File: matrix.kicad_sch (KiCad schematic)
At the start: 285 parts, among them SW2 SW_SPDT, SW3 SW_SPDT

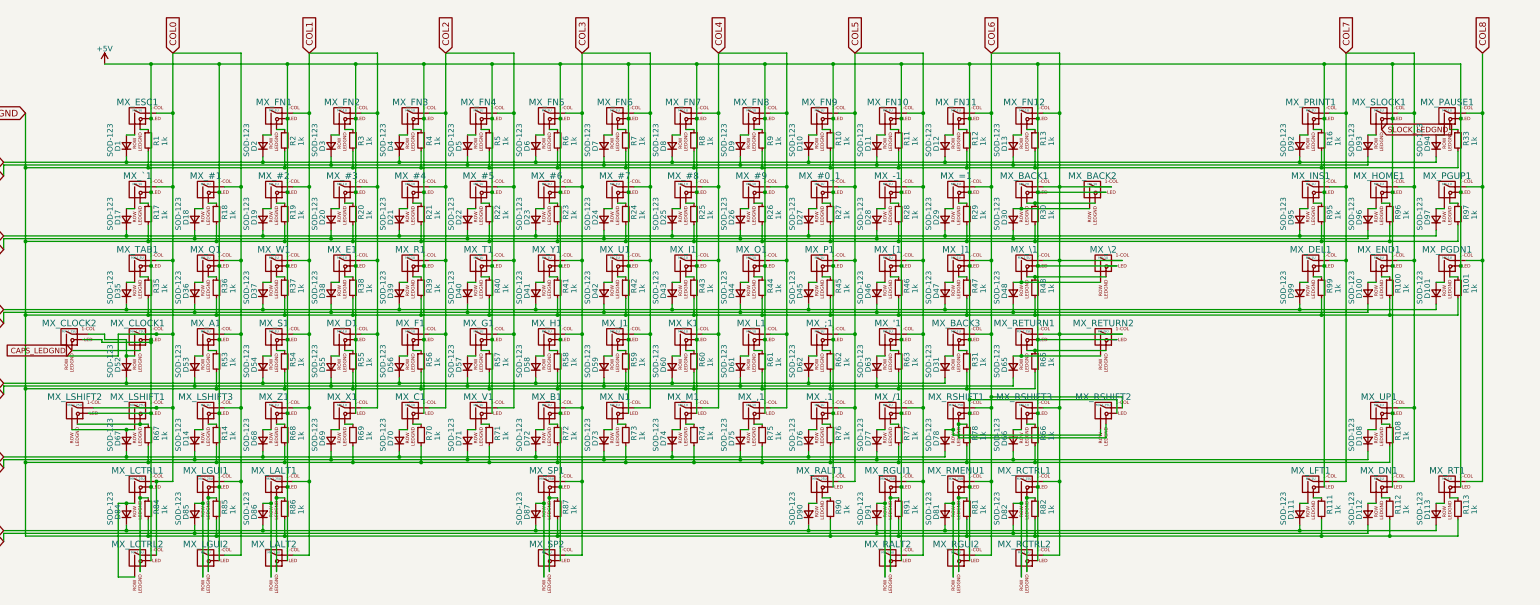
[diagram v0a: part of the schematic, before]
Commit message: Made the project portable
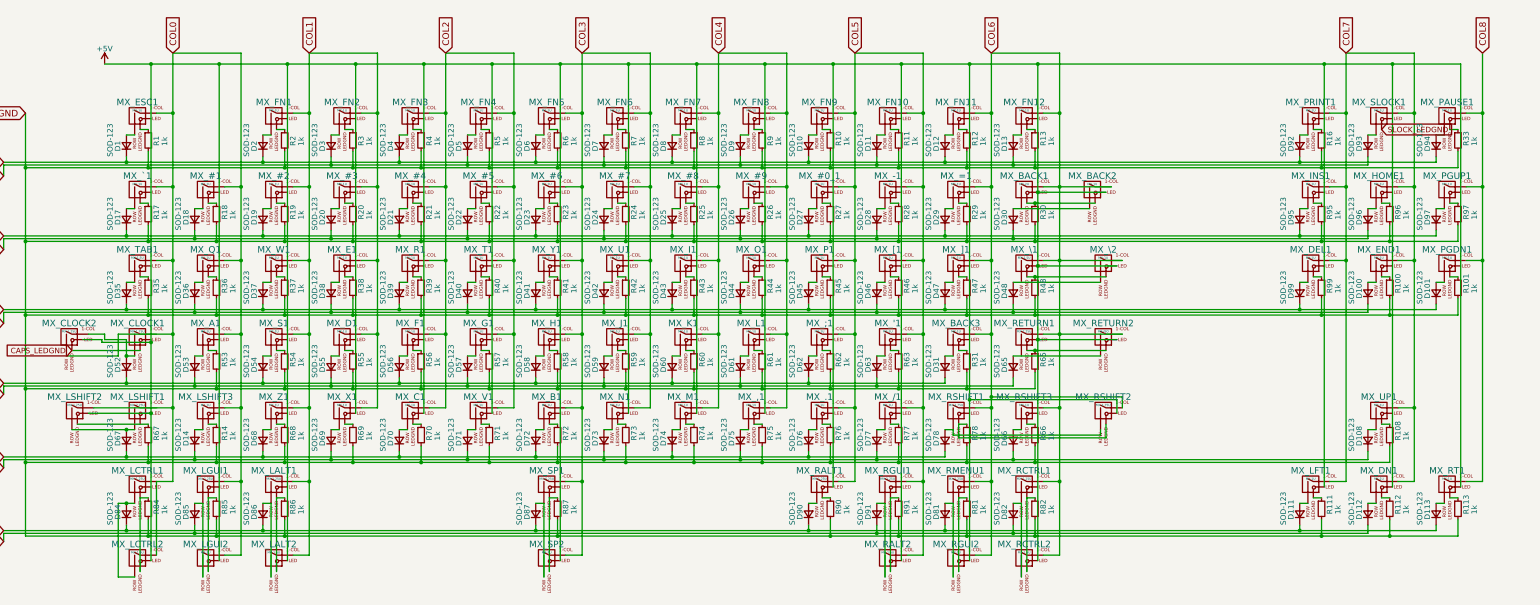
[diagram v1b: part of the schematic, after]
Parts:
- D1, D10, D100, D101, D108, D11, D111, D112, D113, D12, D13, D14, D17, D18, D19, D2, D20, D21, D22, D23, D24, D25, D26, D27, D28, D29, D3, D30, D31, D35, D36, D37, D38, D39, D4, D40, D41, D42, D43, D44, D45, D46, D47, D48, D5, D52, D53, D54, D55, D56, D57, D58, D59, D6, D60, D61, D62, D63, D65, D66, D67, D68, D69, D7, D70, D71, D72, D73, D74, D75, D76, D77, D78, D8, D81, D82, D84, D85, D86, D87, D9, D90, D91, D92, D93, D94, D95, D96, D97, D99: footprint locallib:D_SOD-123 -> KBD8X_MK2_Components:D_SOD-123; symbol Device:D_Small -> KBD8X_MK2_Components:D_Small
- MX_#0_1, MX_#1, MX_#2, MX_#3, MX_#4, MX_#5, MX_#6, MX_#7, MX_#8, MX_#9, MX_'1, MX_,1, MX_-1, MX_.1, MX_/1, MX_;1, MX_=1, MX_A1, MX_B1, MX_BACK2, MX_BACK3, MX_C1, MX_D1, MX_DEL1, MX_DN1, MX_E1, MX_END1, MX_ESC1, MX_F1, MX_FN1, MX_FN10, MX_FN11, MX_FN12, MX_FN2, MX_FN3, MX_FN4, MX_FN5, MX_FN6, MX_FN7, MX_FN8, MX_FN9, MX_G1, MX_H1, MX_HOME1, MX_I1, MX_INS1, MX_J1, MX_K1, MX_L1, MX_LFT1, MX_LSHIFT3, MX_M1, MX_N1, MX_O1, MX_P1, MX_PAUSE1, MX_PGDN1, MX_PGUP1, MX_PRINT1, MX_Q1, MX_R1, MX_RSHIFT3, MX_RT1, MX_S1, MX_SLOCK1, MX_T1, MX_U1, MX_UP1, MX_V1, MX_W1, MX_X1, MX_Y1, MX_Z1, MX_[1, MX_\2, MX_]1, MX_`1: footprint MX_Alps_Hybrid:MXOnly-1U -> KBD8X_MK2_Switches:MXOnly-1U; symbol MX_Alps_Hybrids:MX-1U -> KBD8X_MK2_Switches:MX-1U
- MX_BACK1: footprint MX_Alps_Hybrid:MXOnly-2U -> KBD8X_MK2_Switches:MXOnly-2U; symbol MX_Alps_Hybrids:MX-2U -> KBD8X_MK2_Switches:MX-2U
- MX_CLOCK1: footprint MX_Alps_Hybrid:MXOnly-1.75U -> KBD8X_MK2_Switches:MXOnly-1.75U; symbol MX_Alps_Hybrids:MX-1.75U -> KBD8X_MK2_Switches:MX-1.75U
- MX_CLOCK2, MX_RGUI1: footprint MX_Alps_Hybrid:MXOnly-1.25U-FLIPPED -> KBD8X_MK2_Switches:MXOnly-1.25U-FLIPPED; symbol MX_Alps_Hybrids:MX-1.25U -> KBD8X_MK2_Switches:MX-1.25U
- MX_LALT1, MX_LGUI1, MX_RALT1: footprint MX_Alps_Hybrid:MXOnly-1.25U -> KBD8X_MK2_Switches:MXOnly-1.25U; symbol MX_Alps_Hybrids:MX-1.25U -> KBD8X_MK2_Switches:MX-1.25U
- MX_LALT2, MX_LCTRL2: footprint MX_Alps_Hybrid:MXOnly-1.5U-FLIPPED -> KBD8X_MK2_Switches:MXOnly-1.5U-FLIPPED; symbol MX_Alps_Hybrids:MX-1.5U -> KBD8X_MK2_Switches:MX-1.5U
- MX_LCTRL1: footprint MX_Alps_Hybrid:MXOnly-1.25U -> KBD8X_MK2_Switches:MXOnly-1.25U; symbol MX_Alps_Hybrids:MX-1U -> KBD8X_MK2_Switches:MX-1U
- MX_LGUI2: footprint MX_Alps_Hybrid:MXOnly-1U-FLIPPED -> KBD8X_MK2_Switches:MXOnly-1U-FLIPPED; symbol MX_Alps_Hybrids:MX-1.5U -> KBD8X_MK2_Switches:MX-1.5U
- MX_LSHIFT1, MX_RETURN1: footprint MX_Alps_Hybrid:MXOnly-2.25U -> KBD8X_MK2_Switches:MXOnly-2.25U; symbol MX_Alps_Hybrids:MX-2.25U -> KBD8X_MK2_Switches:MX-2.25U
- MX_LSHIFT2: footprint MX_Alps_Hybrid:MXOnly-1.25U -> KBD8X_MK2_Switches:MXOnly-1.25U; symbol MX_Alps_Hybrids:MX-2.25U -> KBD8X_MK2_Switches:MX-2.25U
- MX_RALT2, MX_RCTRL2, MX_TAB1, MX_\1: footprint MX_Alps_Hybrid:MXOnly-1.5U -> KBD8X_MK2_Switches:MXOnly-1.5U; symbol MX_Alps_Hybrids:MX-1.5U -> KBD8X_MK2_Switches:MX-1.5U
- MX_RCTRL1, MX_RMENU1: footprint MX_Alps_Hybrid:MXOnly-1.25U-FLIPPED -> KBD8X_MK2_Switches:MXOnly-1.25U-FLIPPED; symbol MX_Alps_Hybrids:MX-1U -> KBD8X_MK2_Switches:MX-1U
- MX_RETURN2: footprint MX_Alps_Hybrid:MXOnly-ISO-ROTATED-ReversedStabilizers -> KBD8X_MK2_Switches:MXOnly-ISO-ROTATED-ReversedStabilizers; symbol MX_Alps_Hybrids:MX-2.25U -> KBD8X_MK2_Switches:MX-2.25U
- MX_RGUI2: footprint MX_Alps_Hybrid:MXOnly-1U -> KBD8X_MK2_Switches:MXOnly-1U; symbol MX_Alps_Hybrids:MX-1.5U -> KBD8X_MK2_Switches:MX-1.5U
- MX_RSHIFT1: footprint MX_Alps_Hybrid:MXOnly-2.75U -> KBD8X_MK2_Switches:MXOnly-2.75U; symbol MX_Alps_Hybrids:MX-1U -> KBD8X_MK2_Switches:MX-1U
- MX_RSHIFT2: footprint MX_Alps_Hybrid:MXOnly-1.75U -> KBD8X_MK2_Switches:MXOnly-1.75U; symbol MX_Alps_Hybrids:MX-1U -> KBD8X_MK2_Switches:MX-1U
- MX_SP1: footprint MX_Alps_Hybrid:MXOnly-6.25U-ReversedStabilizers -> KBD8X_MK2_Switches:MXOnly-6.25U-ReversedStabilizers; symbol MX_Alps_Hybrids:MX-6.25U -> KBD8X_MK2_Switches:MX-6.25U
- MX_SP2: footprint MX_Alps_Hybrid:MXOnly-7U-ReversedStabilizers -> KBD8X_MK2_Switches:MXOnly-7U-ReversedStabilizers; symbol MX_Alps_Hybrids:MX-7U -> KBD8X_MK2_Switches:MX-7U
- R1, R10, R100, R101, R108, R11, R111, R112, R113, R12, R13, R14, R16, R17, R18, R19, R2, R20, R21, R22, R23, R24, R25, R26, R27, R28, R29, R3, R30, R31, R32, R33, R35, R36, R37, R38, R39, R4, R40, R41, R42, R43, R44, R45, R46, R47, R48, R5, R52, R53, R54, R55, R56, R57, R58, R59, R6, R60, R61, R62, R63, R65, R66, R67, R68, R69, R7, R70, R71, R72, R73, R74, R75, R76, R77, R78, R8, R81, R82, R84, R85, R86, R87, R9, R90, R91, R95, R96, R97, R99: footprint locallib:R_0603 -> KBD8X_MK2_Components:R_0603; symbol Device:R_Small -> KBD8X_MK2_Components:R_Small
- SW2, SW3: footprint Buttons_Switches_SMD:SW_SPDT_PCM12 -> KBD8X_MK2_Components:SW_SPDT_PCM12; symbol Switch:SW_SPDT -> KBD8X_MK2_Components:SW_SPDT
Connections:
- net +5V: no longer MX_#0_1.3 (LED), MX_#1.3 (LED), MX_#2.3 (LED), MX_#3.3 (LED), MX_#4.3 (LED), MX_#5.3 (LED), MX_#6.3 (LED), MX_#7.3 (LED), MX_#8.3 (LED), MX_#9.3 (LED), MX_'1.3 (LED), MX_-1.3 (LED), MX_.1.3 (LED), MX_/1.3 (LED), MX_;1.3 (LED), MX_=1.3 (LED), MX_A1.3 (LED), MX_B1.3 (LED), MX_BACK3.3 (LED), MX_CLOCK1.3 (LED), MX_D1.3 (LED), MX_DEL1.3 (LED), MX_E1.3 (LED), MX_END1.3 (LED), MX_ESC1.3 (LED), MX_F1.3 (LED), MX_FN1.3 (LED), MX_FN10.3 (LED), MX_FN11.3 (LED), MX_FN12.3 (LED), MX_FN2.3 (LED), MX_FN3.3 (LED), MX_FN4.3 (LED), MX_FN5.3 (LED), MX_FN6.3 (LED), MX_FN7.3 (LED), MX_FN8.3 (LED), MX_FN9.3 (LED), MX_G1.3 (LED), MX_H1.3 (LED), MX_HOME1.3 (LED), MX_I1.3 (LED), MX_INS1.3 (LED), MX_J1.3 (LED), MX_K1.3 (LED), MX_L1.3 (LED), MX_LALT1.3 (LED), MX_LCTRL1.3 (LED), MX_LGUI1.3 (LED), MX_LSHIFT3.3 (LED), MX_O1.3 (LED), MX_P1.3 (LED), MX_PAUSE1.3 (LED), MX_PGDN1.3 (LED), MX_PGUP1.3 (LED), MX_PRINT1.3 (LED), MX_Q1.3 (LED), MX_R1.3 (LED), MX_RCTRL1.3 (LED), MX_RGUI1.3 (LED), MX_RMENU1.3 (LED), MX_RSHIFT1.3 (LED), MX_RSHIFT3.3 (LED), MX_S1.3 (LED), MX_SLOCK1.3 (LED), MX_SP1.3 (LED), MX_T1.3 (LED), MX_TAB1.3 (LED), MX_U1.3 (LED), MX_UP1.3 (LED), MX_W1.3 (LED), MX_Y1.3 (LED), MX_Z1.3 (LED), MX_[1.3 (LED), MX_]1.3 (LED), MX_`1.3 (LED)
- net COL0: no longer MX_CLOCK1.1 (COL), MX_LSHIFT1.1 (COL)
- net at D30.2 (A), MX_BACK2.2 (ROW): no longer MX_BACK1.2 (ROW)
- net at D48.2 (A), MX_\2.2 (ROW): no longer MX_\1.2 (ROW)
- net at MX_LSHIFT2.4 (LEDGND), R67.1: no longer MX_LSHIFT1.4 (LEDGND)
- net at D65.2 (A), MX_RETURN2.2 (ROW): no longer MX_RETURN1.2 (ROW)

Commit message: Rearrenged schematics items
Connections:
- net +5V: now also MX_#0_1.3 (LED), MX_#1.3 (LED), MX_#2.3 (LED), MX_#3.3 (LED), MX_#4.3 (LED), MX_#5.3 (LED), MX_#6.3 (LED), MX_#7.3 (LED), MX_#8.3 (LED), MX_#9.3 (LED), MX_'1.3 (LED), MX_-1.3 (LED), MX_.1.3 (LED), MX_/1.3 (LED), MX_;1.3 (LED), MX_=1.3 (LED), MX_A1.3 (LED), MX_B1.3 (LED), MX_BACK3.3 (LED), MX_CLOCK1.3 (LED), MX_D1.3 (LED), MX_DEL1.3 (LED), MX_E1.3 (LED), MX_END1.3 (LED), MX_ESC1.3 (LED), MX_F1.3 (LED), MX_FN1.3 (LED), MX_FN10.3 (LED), MX_FN11.3 (LED), MX_FN12.3 (LED), MX_FN2.3 (LED), MX_FN3.3 (LED), MX_FN4.3 (LED), MX_FN5.3 (LED), MX_FN6.3 (LED), MX_FN7.3 (LED), MX_FN8.3 (LED), MX_FN9.3 (LED), MX_G1.3 (LED), MX_H1.3 (LED), MX_HOME1.3 (LED), MX_I1.3 (LED), MX_INS1.3 (LED), MX_J1.3 (LED), MX_K1.3 (LED), MX_L1.3 (LED), MX_LALT1.3 (LED), MX_LCTRL1.3 (LED), MX_LGUI1.3 (LED), MX_LSHIFT3.3 (LED), MX_O1.3 (LED), MX_P1.3 (LED), MX_PAUSE1.3 (LED), MX_PGDN1.3 (LED), MX_PGUP1.3 (LED), MX_PRINT1.3 (LED), MX_Q1.3 (LED), MX_R1.3 (LED), MX_RCTRL1.3 (LED), MX_RGUI1.3 (LED), MX_RMENU1.3 (LED), MX_RSHIFT1.3 (LED), MX_RSHIFT3.3 (LED), MX_S1.3 (LED), MX_SLOCK1.3 (LED), MX_SP1.3 (LED), MX_T1.3 (LED), MX_TAB1.3 (LED), MX_U1.3 (LED), MX_UP1.3 (LED), MX_W1.3 (LED), MX_Y1.3 (LED), MX_Z1.3 (LED), MX_[1.3 (LED), MX_]1.3 (LED), MX_`1.3 (LED)
- net COL0: now also MX_CLOCK1.1 (COL), MX_LSHIFT1.1 (COL)
- net at MX_BACK1.2 (ROW): now also D30.2 (A), MX_BACK2.2 (ROW)
- net at MX_\1.2 (ROW): now also D48.2 (A), MX_\2.2 (ROW)
- net at MX_LSHIFT1.4 (LEDGND): now also MX_LSHIFT2.4 (LEDGND), R67.1
- net at MX_RETURN1.2 (ROW): now also D65.2 (A), MX_RETURN2.2 (ROW)
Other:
- moved on the sheet: D1, D10, D100, D101, D108, D11, D111, D112, D113, D12, D13, D14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

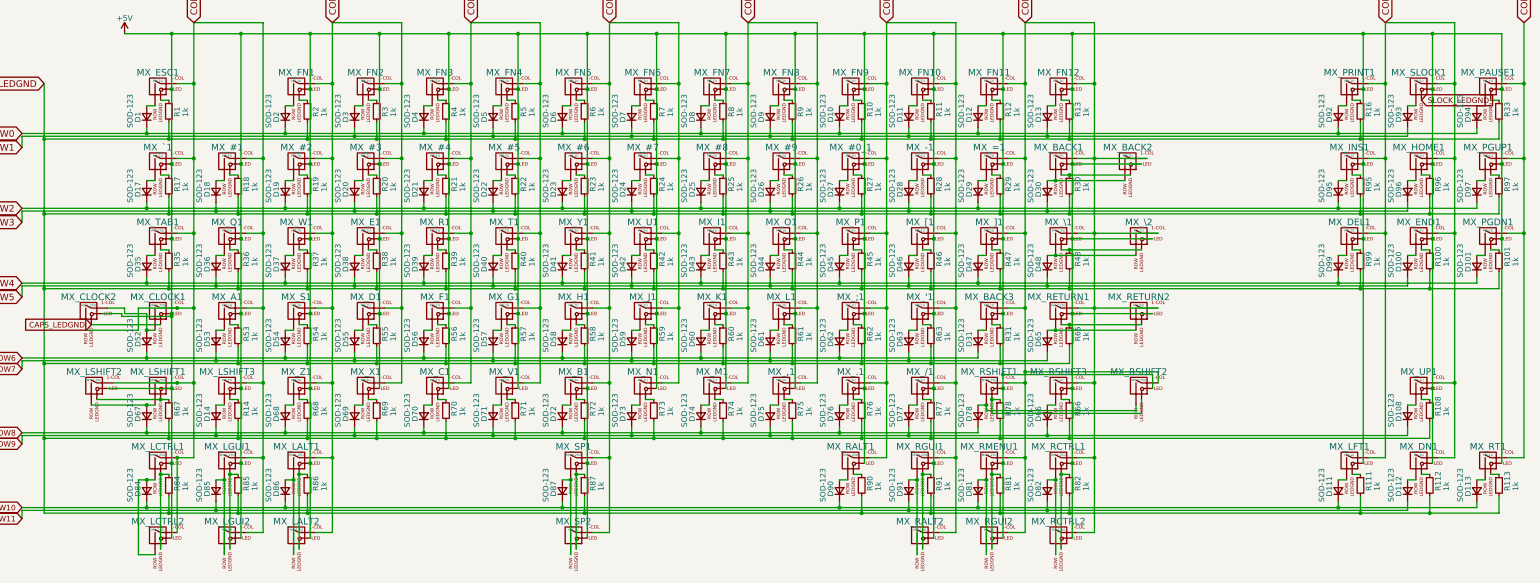
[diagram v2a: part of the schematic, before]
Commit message: Updated symbols used in the schematics
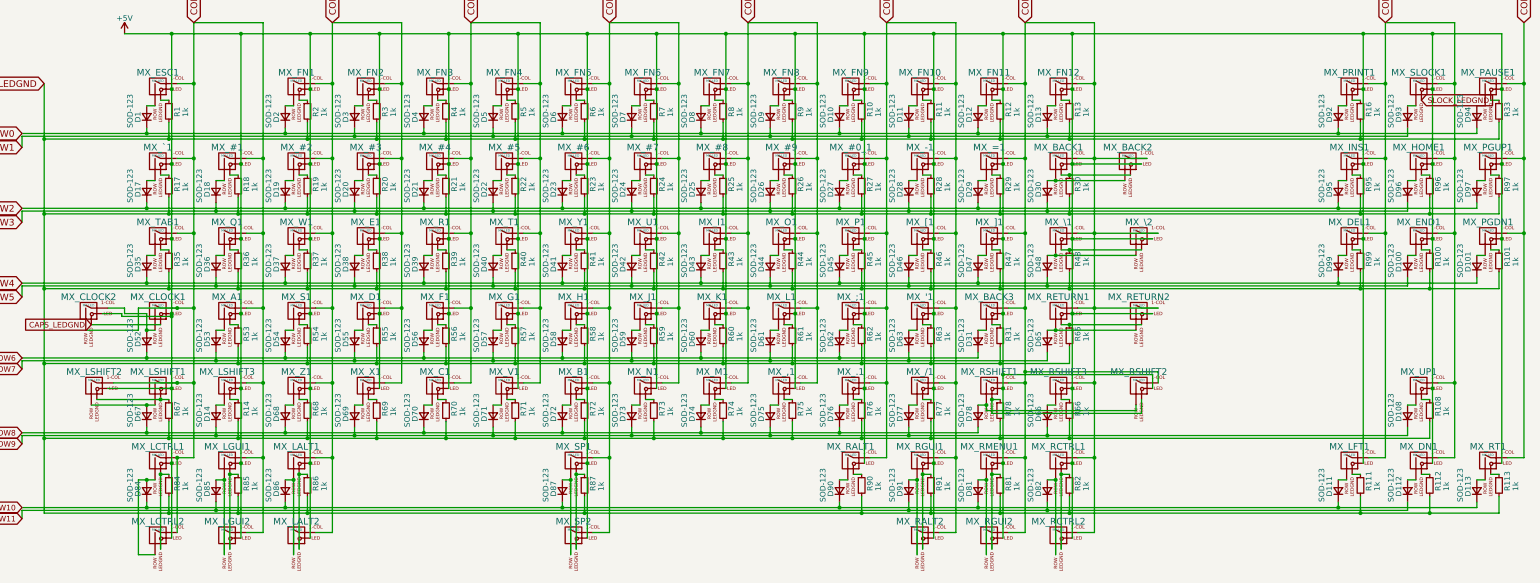
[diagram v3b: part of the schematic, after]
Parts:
- MX_#0_1, MX_#1, MX_#2, MX_#3, MX_#4, MX_#5, MX_#6, MX_#7, MX_#8, MX_#9, MX_'1, MX_,1, MX_-1, MX_.1, MX_/1, MX_;1, MX_=1, MX_A1, MX_B1, MX_BACK2, MX_BACK3, MX_C1, MX_D1, MX_DEL1, MX_DN1, MX_E1, MX_END1, MX_ESC1, MX_F1, MX_FN1, MX_FN10, MX_FN11, MX_FN12, MX_FN2, MX_FN3, MX_FN4, MX_FN5, MX_FN6, MX_FN7, MX_FN8, MX_FN9, MX_G1, MX_H1, MX_HOME1, MX_I1, MX_INS1, MX_J1, MX_K1, MX_L1, MX_LFT1, MX_LSHIFT3, MX_M1, MX_N1, MX_O1, MX_P1, MX_PAUSE1, MX_PGDN1, MX_PGUP1, MX_PRINT1, MX_Q1, MX_R1, MX_RSHIFT3, MX_RT1, MX_S1, MX_SLOCK1, MX_T1, MX_U1, MX_UP1, MX_V1, MX_W1, MX_X1, MX_Y1, MX_Z1, MX_[1, MX_\2, MX_]1, MX_`1: value MX-1U -> MX-LED; symbol KBD8X_MK2_Switches:MX-1U -> KBD8X_MK2_Switches:MX-LED
- MX_BACK1: value MX-2U -> MX-LED; symbol KBD8X_MK2_Switches:MX-2U -> KBD8X_MK2_Switches:MX-LED
- MX_CLOCK1: value MX-1.75U -> MX-LED; symbol KBD8X_MK2_Switches:MX-1.75U -> KBD8X_MK2_Switches:MX-LED
- MX_CLOCK2, MX_LALT1, MX_LGUI1, MX_RALT1, MX_RGUI1: value MX-1.25U -> MX-LED; symbol KBD8X_MK2_Switches:MX-1.25U -> KBD8X_MK2_Switches:MX-LED
- MX_LALT2, MX_LCTRL2, MX_RALT2, MX_RCTRL2, MX_TAB1, MX_\1: value MX-1.5U -> MX-LED; symbol KBD8X_MK2_Switches:MX-1.5U -> KBD8X_MK2_Switches:MX-LED
- MX_LCTRL1, MX_RCTRL1, MX_RMENU1: value MX-1.25U -> MX-LED; symbol KBD8X_MK2_Switches:MX-1U -> KBD8X_MK2_Switches:MX-LED
- MX_LGUI2, MX_RGUI2: value MX-1U -> MX-LED; symbol KBD8X_MK2_Switches:MX-1.5U -> KBD8X_MK2_Switches:MX-LED
- MX_LSHIFT1, MX_RETURN1: value MX-2.25U -> MX-LED; symbol KBD8X_MK2_Switches:MX-2.25U -> KBD8X_MK2_Switches:MX-LED
- MX_LSHIFT2: value MX-1.25U -> MX-LED; symbol KBD8X_MK2_Switches:MX-2.25U -> KBD8X_MK2_Switches:MX-LED
- MX_RETURN2: value MX-ISO -> MX-LED; symbol KBD8X_MK2_Switches:MX-2.25U -> KBD8X_MK2_Switches:MX-LED
- MX_RSHIFT1: value MX-2.75U -> MX-LED; symbol KBD8X_MK2_Switches:MX-1U -> KBD8X_MK2_Switches:MX-LED
- MX_RSHIFT2: value MX-1.75U -> MX-LED; symbol KBD8X_MK2_Switches:MX-1U -> KBD8X_MK2_Switches:MX-LED
- MX_SP1: value MX-6.25U -> MX-LED; symbol KBD8X_MK2_Switches:MX-6.25U -> KBD8X_MK2_Switches:MX-LED
- MX_SP2: value MX-7U -> MX-LED; symbol KBD8X_MK2_Switches:MX-7U -> KBD8X_MK2_Switches:MX-LED

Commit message: Removed leds and unnecessary resistors
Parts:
- removed R1, R10, R100, R101, R108, R11, R111, R112, R113, R12, R13, R14, R16, R17, R18, R19, R2, R20, R21, R22, R23, R24, R25, R26, R27, R28, R29, R3, R30, R31, R33, R35, R36, R37, R38, R39, R4, R40, R41, R42, R43, R44, R45, R46, R47, R48, R5, R53, R54, R55, R56, R57, R58, R59, R6, R60, R61, R62, R63, R65, R66, R67, R68, R69, R7, R70, R71, R72, R73, R74, R75, R76, R77, R78, R8, R81, R82, R84, R85, R86, R87, R9, R90, R91, R95, R96, R97, R99: 1k, KBD8X_MK2_Components:R_0603, symbol KBD8X_MK2_Components:R_Small
- removed SW2, SW3: SW_SPDT, KBD8X_MK2_Components:SW_SPDT_PCM12, symbol KBD8X_MK2_Components:SW_SPDT
- MX_#0_1, MX_#1, MX_#2, MX_#3, MX_#4, MX_#5, MX_#6, MX_#7, MX_#8, MX_#9, MX_'1, MX_,1, MX_-1, MX_.1, MX_/1, MX_;1, MX_=1, MX_A1, MX_B1, MX_BACK2, MX_BACK3, MX_C1, MX_D1, MX_DEL1, MX_DN1, MX_E1, MX_END1, MX_ESC1, MX_F1, MX_FN1, MX_FN10, MX_FN11, MX_FN12, MX_FN2, MX_FN3, MX_FN4, MX_FN5, MX_FN6, MX_FN7, MX_FN8, MX_FN9, MX_G1, MX_H1, MX_HOME1, MX_I1, MX_INS1, MX_J1, MX_K1, MX_L1, MX_LFT1, MX_LSHIFT3, MX_M1, MX_N1, MX_O1, MX_P1, MX_PAUSE1, MX_PGDN1, MX_PGUP1, MX_PRINT1, MX_Q1, MX_R1, MX_RGUI2, MX_RSHIFT3, MX_RT1, MX_S1, MX_T1, MX_U1, MX_UP1, MX_V1, MX_W1, MX_X1, MX_Y1, MX_Z1, MX_[1, MX_\2, MX_]1, MX_`1: value MX-LED -> MX-NoLED; footprint KBD8X_MK2_Switches:MXOnly-1U -> KBD8X_MK2_Switches:MXOnly-1U-NoLED; symbol KBD8X_MK2_Switches:MX-LED -> KBD8X_MK2_Switches:MX-NoLED
- MX_BACK1: value MX-LED -> MX-NoLED; footprint KBD8X_MK2_Switches:MXOnly-2U -> KBD8X_MK2_Switches:MXOnly-2U-NoLED; symbol KBD8X_MK2_Switches:MX-LED -> KBD8X_MK2_Switches:MX-NoLED
- MX_LALT1, MX_LCTRL1, MX_LGUI1, MX_LSHIFT2, MX_RALT1: value MX-LED -> MX-NoLED; footprint KBD8X_MK2_Switches:MXOnly-1.25U -> KBD8X_MK2_Switches:MXOnly-1.25U-NoLED; symbol KBD8X_MK2_Switches:MX-LED -> KBD8X_MK2_Switches:MX-NoLED
- MX_LALT2, MX_LCTRL2: value MX-LED -> MX-NoLED; footprint KBD8X_MK2_Switches:MXOnly-1.5U-FLIPPED -> KBD8X_MK2_Switches:MXOnly-1.5U-NoLED; symbol KBD8X_MK2_Switches:MX-LED -> KBD8X_MK2_Switches:MX-NoLED
- MX_LGUI2: value MX-LED -> MX-NoLED; footprint KBD8X_MK2_Switches:MXOnly-1U-FLIPPED -> KBD8X_MK2_Switches:MXOnly-1U-NoLED; symbol KBD8X_MK2_Switches:MX-LED -> KBD8X_MK2_Switches:MX-NoLED
- MX_LSHIFT1, MX_RETURN1: value MX-LED -> MX-NoLED; footprint KBD8X_MK2_Switches:MXOnly-2.25U -> KBD8X_MK2_Switches:MXOnly-2.25U-NoLED; symbol KBD8X_MK2_Switches:MX-LED -> KBD8X_MK2_Switches:MX-NoLED
- MX_RALT2, MX_RCTRL2, MX_TAB1, MX_\1: value MX-LED -> MX-NoLED; footprint KBD8X_MK2_Switches:MXOnly-1.5U -> KBD8X_MK2_Switches:MXOnly-1.5U-NoLED; symbol KBD8X_MK2_Switches:MX-LED -> KBD8X_MK2_Switches:MX-NoLED
- MX_RCTRL1, MX_RGUI1, MX_RMENU1: value MX-LED -> MX-NoLED; footprint KBD8X_MK2_Switches:MXOnly-1.25U-FLIPPED -> KBD8X_MK2_Switches:MXOnly-1.25U-NoLED; symbol KBD8X_MK2_Switches:MX-LED -> KBD8X_MK2_Switches:MX-NoLED
- MX_RETURN2: value MX-LED -> MX-NoLED; footprint KBD8X_MK2_Switches:MXOnly-ISO-ROTATED-ReversedStabilizers -> KBD8X_MK2_Switches:MXOnly-ISO-ROTATED-ReversedStabilizers-NoLED; symbol KBD8X_MK2_Switches:MX-LED -> KBD8X_MK2_Switches:MX-NoLED
- MX_RSHIFT1: value MX-LED -> MX-NoLED; footprint KBD8X_MK2_Switches:MXOnly-2.75U -> KBD8X_MK2_Switches:MXOnly-2.75U-NoLED; symbol KBD8X_MK2_Switches:MX-LED -> KBD8X_MK2_Switches:MX-NoLED
- MX_RSHIFT2: value MX-LED -> MX-NoLED; footprint KBD8X_MK2_Switches:MXOnly-1.75U -> KBD8X_MK2_Switches:MXOnly-1.75U-NoLED; symbol KBD8X_MK2_Switches:MX-LED -> KBD8X_MK2_Switches:MX-NoLED
- MX_SP1: value MX-LED -> MX-NoLED; footprint KBD8X_MK2_Switches:MXOnly-6.25U-ReversedStabilizers -> KBD8X_MK2_Switches:MXOnly-6.25U-ReversedStabilizers-NoLED; symbol KBD8X_MK2_Switches:MX-LED -> KBD8X_MK2_Switches:MX-NoLED
- MX_SP2: value MX-LED -> MX-NoLED; footprint KBD8X_MK2_Switches:MXOnly-7U-ReversedStabilizers -> KBD8X_MK2_Switches:MXOnly-7U-ReversedStabilizers-NoLED; symbol KBD8X_MK2_Switches:MX-LED -> KBD8X_MK2_Switches:MX-NoLED
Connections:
- net +5V: no longer MX_#0_1.3 (LED), MX_#1.3 (LED), MX_#2.3 (LED), MX_#3.3 (LED), MX_#4.3 (LED), MX_#5.3 (LED), MX_#6.3 (LED), MX_#7.3 (LED), MX_#8.3 (LED), MX_#9.3 (LED), MX_'1.3 (LED), MX_,1.3 (LED), MX_-1.3 (LED), MX_.1.3 (LED), MX_/1.3 (LED), MX_;1.3 (LED), MX_=1.3 (LED), MX_A1.3 (LED), MX_B1.3 (LED), MX_BACK1.3 (LED), MX_BACK2.3 (LED), MX_BACK3.3 (LED), MX_C1.3 (LED), MX_D1.3 (LED), MX_DEL1.3 (LED), MX_DN1.3 (LED), MX_E1.3 (LED), MX_END1.3 (LED), MX_ESC1.3 (LED), MX_F1.3 (LED), MX_FN1.3 (LED), MX_FN10.3 (LED), MX_FN11.3 (LED), MX_FN12.3 (LED), MX_FN2.3 (LED), MX_FN3.3 (LED), MX_FN4.3 (LED), MX_FN5.3 (LED), MX_FN6.3 (LED), MX_FN7.3 (LED), MX_FN8.3 (LED), MX_FN9.3 (LED), MX_G1.3 (LED), MX_H1.3 (LED), MX_HOME1.3 (LED), MX_I1.3 (LED), MX_INS1.3 (LED), MX_J1.3 (LED), MX_K1.3 (LED), MX_L1.3 (LED), MX_LALT1.3 (LED), MX_LALT2.3 (LED), MX_LCTRL1.3 (LED), MX_LCTRL2.3 (LED), MX_LFT1.3 (LED), MX_LGUI1.3 (LED), MX_LGUI2.3 (LED), MX_LSHIFT1.3 (LED), MX_LSHIFT2.3 (LED), MX_LSHIFT3.3 (LED), MX_M1.3 (LED), MX_N1.3 (LED), MX_O1.3 (LED), MX_P1.3 (LED), MX_PAUSE1.3 (LED), MX_PGDN1.3 (LED), MX_PGUP1.3 (LED), MX_PRINT1.3 (LED), MX_Q1.3 (LED), MX_R1.3 (LED), MX_RALT1.3 (LED), MX_RALT2.3 (LED), MX_RCTRL1.3 (LED), MX_RCTRL2.3 (LED), MX_RETURN1.3 (LED), MX_RETURN2.3 (LED), MX_RGUI1.3 (LED), MX_RGUI2.3 (LED), MX_RMENU1.3 (LED), MX_RSHIFT1.3 (LED), MX_RSHIFT2.3 (LED), MX_RSHIFT3.3 (LED), MX_RT1.3 (LED), MX_S1.3 (LED), MX_SP1.3 (LED), MX_SP2.3 (LED), MX_T1.3 (LED), MX_TAB1.3 (LED), MX_U1.3 (LED), MX_UP1.3 (LED), MX_V1.3 (LED), MX_W1.3 (LED), MX_X1.3 (LED), MX_Y1.3 (LED), MX_Z1.3 (LED), MX_[1.3 (LED), MX_\1.3 (LED), MX_\2.3 (LED), MX_]1.3 (LED), MX_`1.3 (LED)
- net CAPS_IND: now also R52.2
- net SLOCK_IND: now also R32.1
- net CAPS_LEDGND: no longer names the net of MX_CLOCK1.4 (LEDGND), MX_CLOCK2.4 (LEDGND), R52.1
- net SLOCK_LEDGND: no longer names the net of MX_SLOCK1.4 (LEDGND), R32.2
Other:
- moved on the sheet: D1, D10, D100, D101, D108, D11, D111, D112, D113, D12, D13, D14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
